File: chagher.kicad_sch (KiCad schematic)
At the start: 19 parts, among them Q2 AO3401A, U4 LTV-817, U5 LTV-817, U6 CN3763

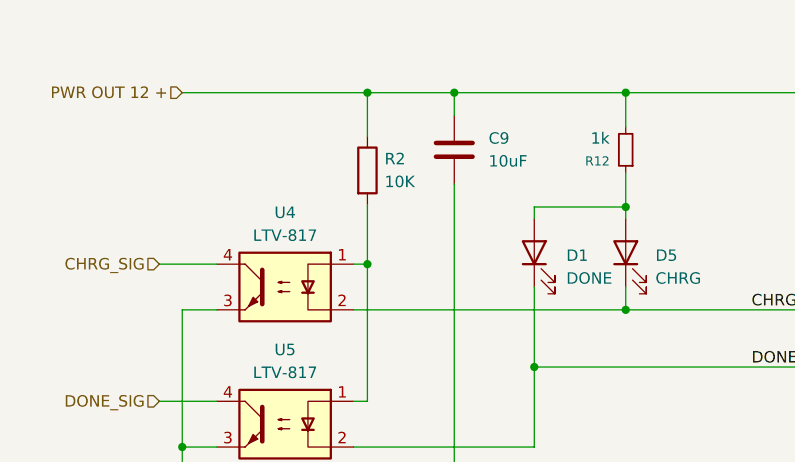
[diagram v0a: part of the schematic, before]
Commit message: Connect srcond relay
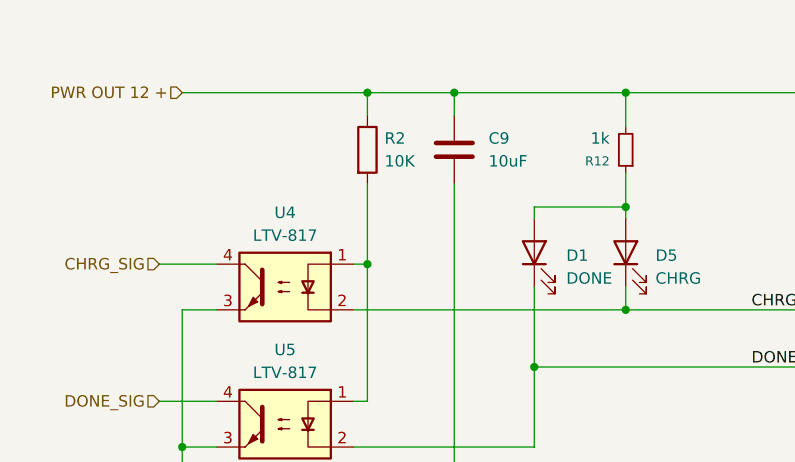
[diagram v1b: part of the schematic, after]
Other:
- moved on the sheet: R2
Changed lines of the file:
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@@
 	(wire
 		(pts
-			(xy 79.756 82.042) (xy 79.756 88.646)
+			(xy 79.756 79.756) (xy 79.756 88.646)
 		)
 		(stroke
@@
 	(wire
 		(pts
-			(xy 79.756 69.596) (xy 79.756 74.422)
+			(xy 79.756 69.596) (xy 79.756 72.136)
 		)
 		(stroke
@@
 	(symbol
 		(lib_id "Device:R")
-		(at 79.756 78.232 0)
+		(at 79.756 75.946 0)
 		(unit 1)
 		(exclude_from_sim no)
@@
 		(fields_autoplaced yes)
 		(property "Reference" "R2"
-			(at 81.661 76.9619 0)
+			(at 81.661 74.6759 0)
 			(effects
 				(font
@@
 		)
 		(property "Value" "10K"
-			(at 81.661 79.5019 0)
+			(at 81.661 77.2159 0)
 			(effects
 				(font
@@
 		)
 		(property "Footprint" "Resistor_SMD:R_0805_2012Metric_Pad1.20x1.40mm_HandSolder"
-			(at 77.978 78.232 90)
+			(at 77.978 75.946 90)
 			(effects
 				(font
@@
 		)
 		(property "Datasheet" "~"
-			(at 79.756 78.232 0)
+			(at 79.756 75.946 0)
 			(effects
 				(font
@@
 		)
 		(property "Description" ""
-			(at 79.756 78.232 0)
+			(at 79.756 75.946 0)
 			(effects
 				(font
@@
 		)
 		(property "descr" ""
-			(at 79.756 78.232 0)
-			(effects
-				(font
+			(at 79.756 75.946 0)
+			(effects
+				(font
